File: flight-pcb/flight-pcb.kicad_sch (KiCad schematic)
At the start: 21 parts

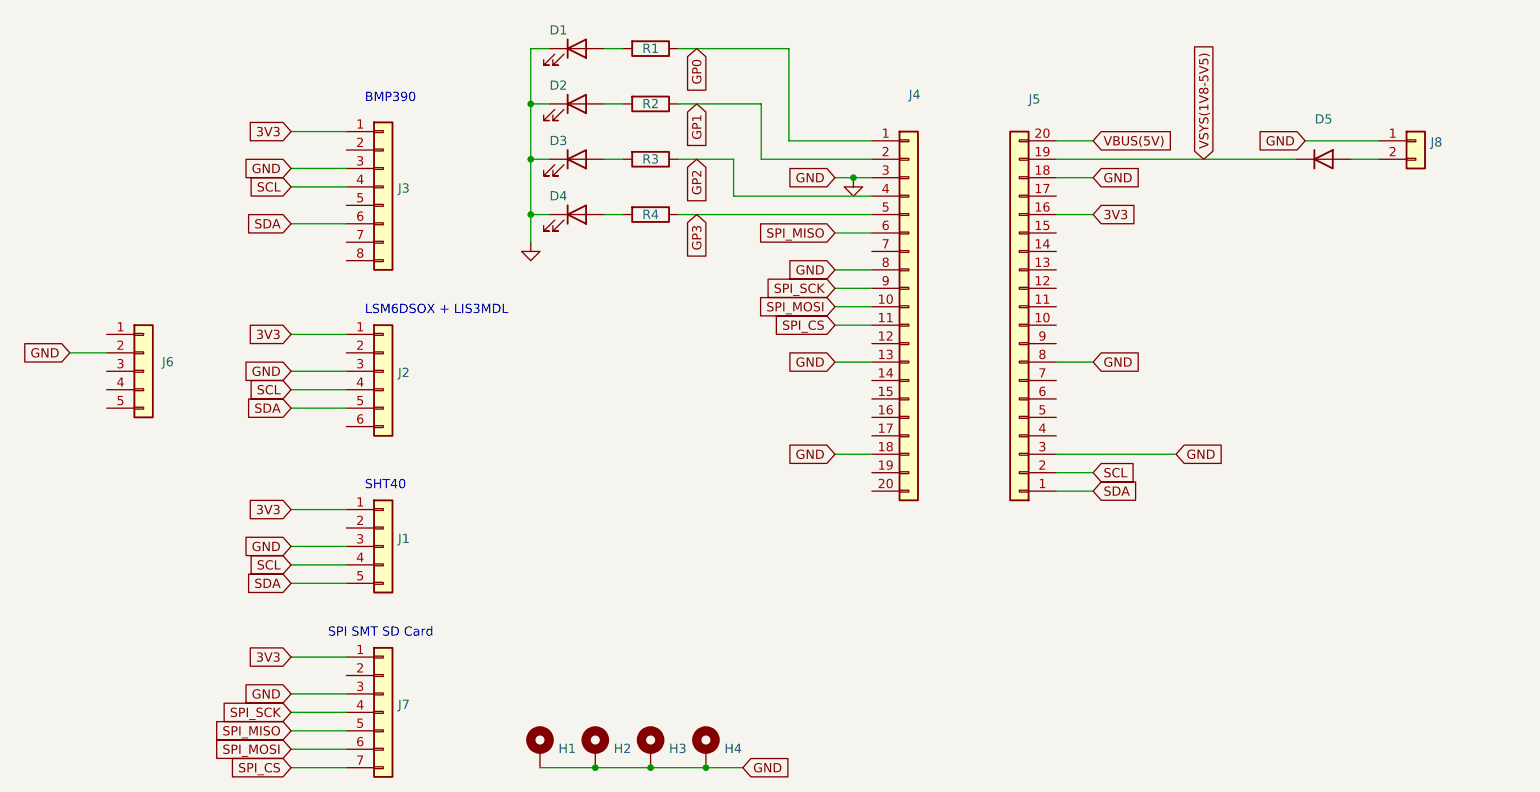
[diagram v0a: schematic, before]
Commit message: updated raspberry pi header pins
updated board to include new library with different pin numbers
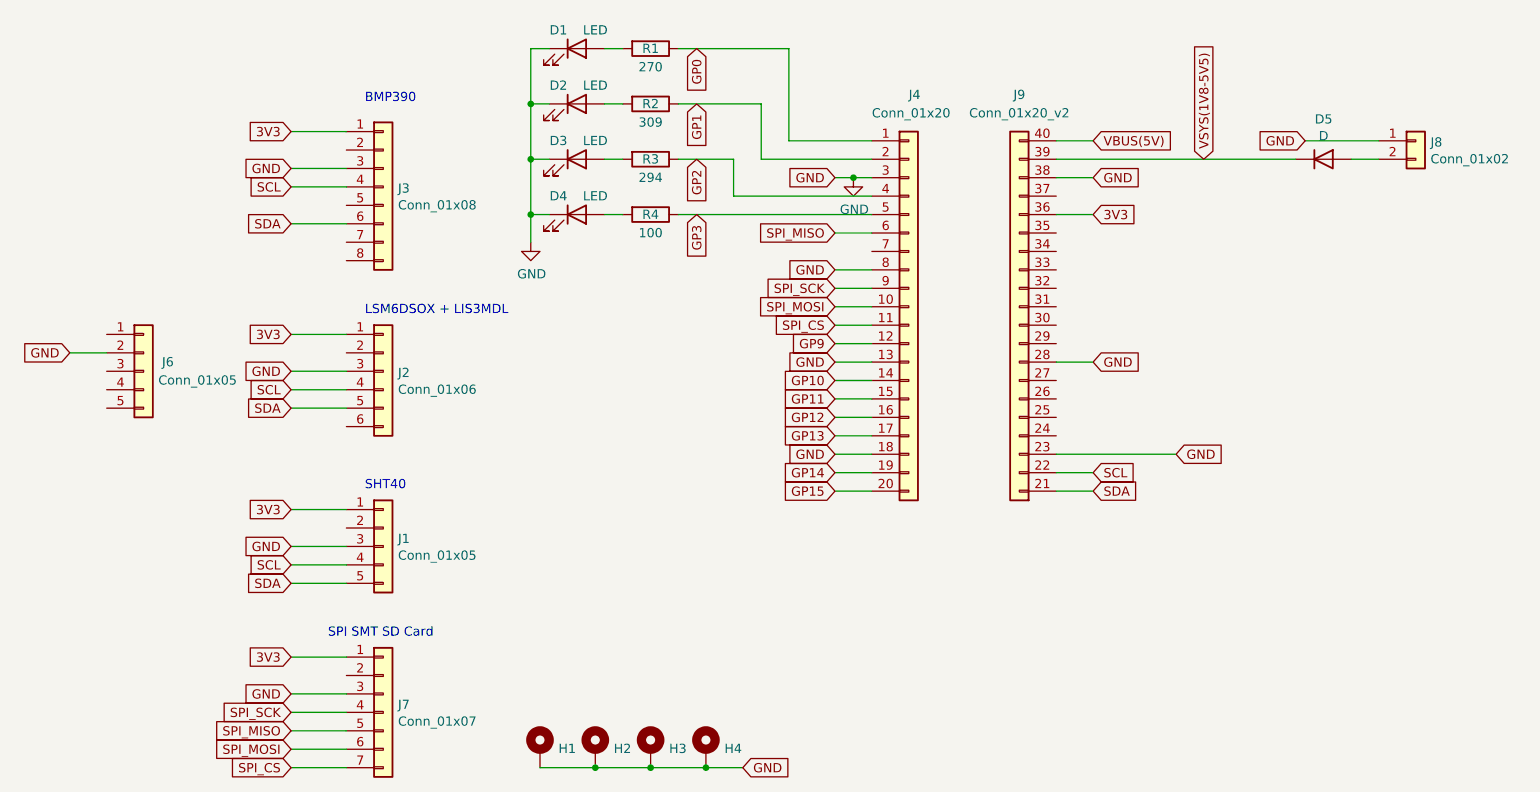
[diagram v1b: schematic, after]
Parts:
- removed J5: (no value), symbol Connector_Generic:Conn_01x20
- added J9: Conn_01x20_v2, Library:PinHeader_1x20_v2_P2.54mm_Vertical, symbol Connector_Generic2:Conn_01x20_v2
- D1, D2, D3, D4: value (none) -> LED; footprint (none) -> LED_SMD:LED_0603_1608Metric
- D5: value (none) -> D; footprint (none) -> Diode_SMD:D_SOD-123F
- H1, H2, H3, H4: value (none) -> MountingHole_Pad; footprint (none) -> MountingHole:MountingHole_2.5mm_Pad
- J1, J6: value (none) -> Conn_01x05; footprint (none) -> Connector_PinHeader_2.54mm:PinHeader_1x05_P2.54mm_Vertical
- J2: value (none) -> Conn_01x06; footprint (none) -> Connector_PinHeader_2.54mm:PinHeader_1x06_P2.54mm_Vertical
- J3: value (none) -> Conn_01x08; footprint (none) -> Connector_PinHeader_2.54mm:PinHeader_1x08_P2.54mm_Vertical
- J4: value (none) -> Conn_01x20; footprint (none) -> Connector_PinHeader_2.54mm:PinHeader_1x20_P2.54mm_Vertical
- J7: value (none) -> Conn_01x07; footprint (none) -> Connector_PinHeader_2.54mm:PinHeader_1x07_P2.54mm_Vertical
- J8: value (none) -> Conn_01x02; footprint (none) -> Connector_JST:JST_PH_S2B-PH-SM4-TB_1x02-1MP_P2.00mm_Horizontal
- R1: value (none) -> 270; footprint (none) -> Resistor_SMD:R_0603_1608Metric
- R2: value (none) -> 309; footprint (none) -> Resistor_SMD:R_0603_1608Metric
- R3: value (none) -> 294; footprint (none) -> Resistor_SMD:R_0603_1608Metric
- R4: value (none) -> 100; footprint (none) -> Resistor_SMD:R_0603_1608Metric
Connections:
- net 3V3: now also J9.36 (Pin_16)
- net GND: now also J9.23 (Pin_3), J9.28 (Pin_8), J9.38 (Pin_18)
- net SCL: now also J9.22 (Pin_2)
- net SDA: now also J9.21 (Pin_1)
- net VBUS(5V): now also J9.40 (Pin_20)
- net VSYS(1V8-5V5): now also J9.39 (Pin_19)
- net GP9: now reaches J4.12 (Pin_12)
- net GP10: now reaches J4.14 (Pin_14)
- net GP11: now reaches J4.15 (Pin_15)
- net GP12: now reaches J4.16 (Pin_16)
- net GP13: now reaches J4.17 (Pin_17)
- net GP14: now reaches J4.19 (Pin_19)
- net GP15: now reaches J4.20 (Pin_20)
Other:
- title: (none) -> flight-pcb
